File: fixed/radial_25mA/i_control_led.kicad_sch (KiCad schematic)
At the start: 14 parts, among them J1 Conn_01x04, J2 Conn_01x04, Q1 MMBT5551L, U1 LM2775DSG, U2 LMV321

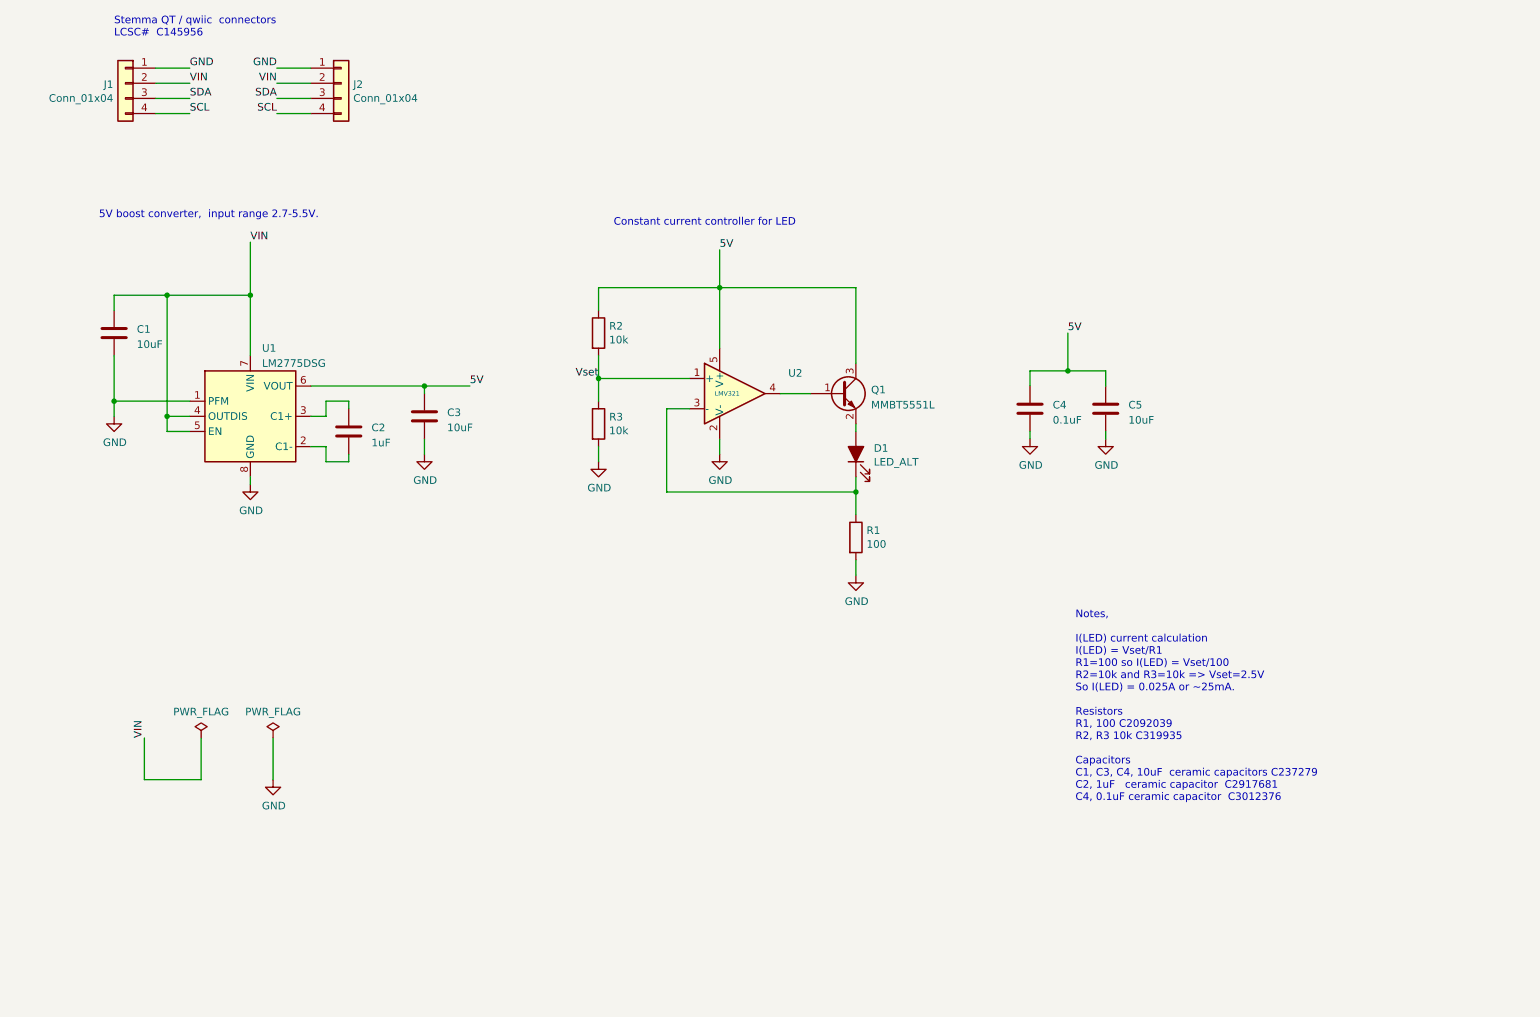
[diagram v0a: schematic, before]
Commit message: Work on rev2 of fixed 25mA radial design.
Finished layout, routing and fab files.
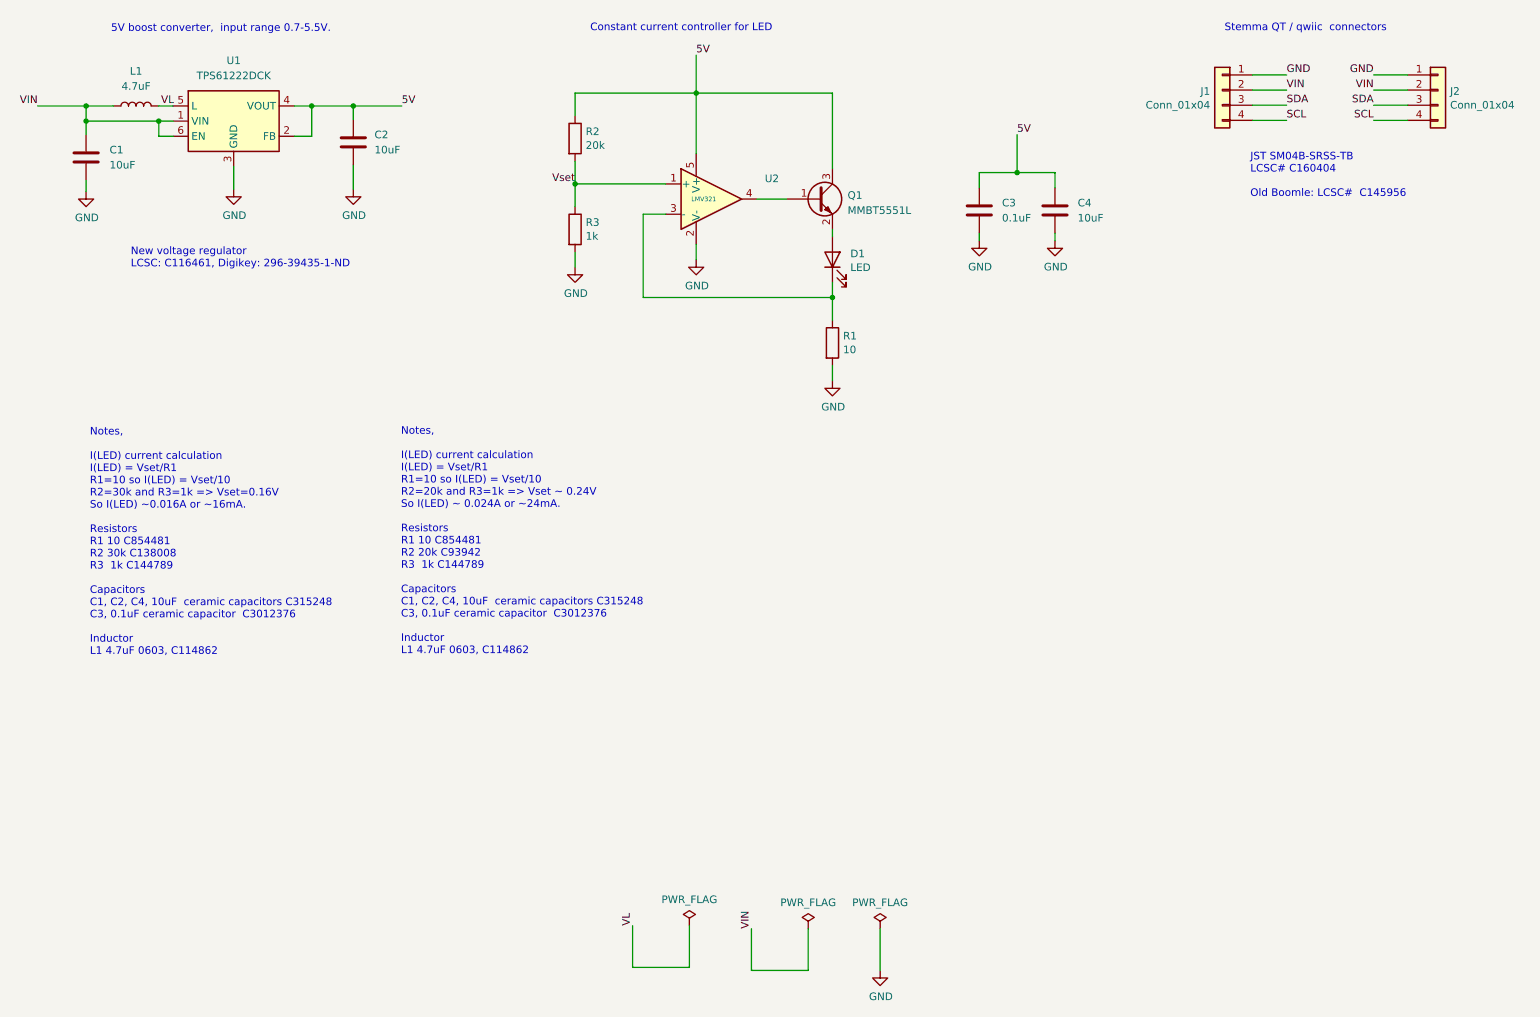
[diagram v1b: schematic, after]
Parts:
- removed C3: 10uF, Capacitor_SMD:C_0402_1005Metric, symbol Device:C
- removed U1: LM2775DSG, Package_SON:WSON-8-1EP_2x2mm_P0.5mm_EP0.9x1.6mm_ThermalVias, symbol Regulator_SwitchedCapacitor:LM2775DSG
- added L1: 4.7uF, Inductor_SMD:L_0603_1608Metric, symbol Device:L
- added U1: TPS61222DCK, Package_TO_SOT_SMD:SOT-363_SC-70-6, symbol Regulator_Switching:TPS61222DCK
- C2: value 1uF -> 10uF
- D1: value LED_ALT -> LED; footprint LED_THT:LED_D3.0mm -> LED_D3mm_custom:LED_D3.0mm; symbol basic_led-rescue:LED_ALT-Device -> Device:LED
- J1, J2: footprint BOOMELE_SH_SMD:BOOMELE_SMD_SH_4PIN_RT -> JST_SH_SM04B_custom:JST_SH_SM04B-SRSS-TB_1x04-1MP_P1.00mm_Horizontal
- R1: value 100 -> 10
- R2: value 10k -> 20k
- R3: value 10k -> 1k
- renumbered C4 to C3, C5 to C4
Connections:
- net 5V: now also C2.2, U1.2 (FB), U1.4 (VOUT)
- net GND: now also C2.1, U1.3 (GND)
- net VIN: now also L1.1, U1.1 (VIN), U1.6 (EN)
- new net VL: L1.2, U1.5 (L)
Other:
- note added: "5V boost converter, input range 0.7-5.5V."
- note added: "JST SM04B-SRSS-TB LCSC# C160404 Old Boomle: LCSC# C145956"
- note added: "New voltage regulator LCSC: C116461, Digikey: 296-39435-1-ND"
- note added: "Notes, I(LED) current calculation I(LED) = Vset/R1 R1=10 so I(LED) = Vset/10 R2=20k and R3=1k => Vset ~ 0.24V So I(LED) ~ 0.024A or ~24mA. Resistors R1 10 C854481 R2 20k C93942 R3 1k C144789 Capacitors C1, C2, C4, 10uF ceramic capacitors C315248 C3, 0.1uF ceramic capacitor C3012376 Inductor L1 4.7uF 0603, C114862"
- note added: "Notes, I(LED) current calculation I(LED) = Vset/R1 R1=10 so I(LED) = Vset/10 R2=30k and R3=1k => Vset=0.16V So I(LED) ~0.016A or ~16mA. Resistors R1 10 C854481 R2 30k C138008 R3 1k C144789 Capacitors C1, C2, C4, 10uF ceramic capacitors C315248 C3, 0.1uF ceramic capacitor C3012376 Inductor L1 4.7uF 0603, C114862"
- note added: "Stemma QT / qwiic connectors"
- note removed: "5V boost converter, input range 2.7-5.5V."
- note removed: "Notes, I(LED) current calculation I(LED) = Vset/R1 R1=100 so I(LED) = Vset/100 R2=10k and R3=10k => Vset=2.5V So I(LED) = 0.025A or ~25mA. Resistors R1, 100 C2092039 R2, R3 10k C319935 Capacitors C1, C3, C4, 10uF ceramic capacitors C237279 C2, 1uF ceramic capacitor C2917681 C4, 0.1uF ceramic capacitor C3012376"
- note removed: "Stemma QT / qwiic connectors LCSC# C145956"
- moved on the sheet: C3, C4, J1, J2, Q1, R1, R2, R3, U2
